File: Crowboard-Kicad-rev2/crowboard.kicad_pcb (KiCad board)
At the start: 2 copper layers, 251.9 x 118.8 mm, 75 parts, among them U1 Pico

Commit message: rev2
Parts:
- added J1: Conn_01x05, other_parts:pimoroni, F.Cu at (149.5, 120.6)
- added SW1: RotaryEncoder, Rotary_Encoder:RotaryEncoder_Alps_EC12E_Vertical_H20mm, F.Cu at (118.9, 112.6)
- added SW2: RotaryEncoder, Rotary_Encoder:RotaryEncoder_Alps_EC12E_Vertical_H20mm, F.Cu at (166.5, 112.7)
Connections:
- U1 pad 16: unconnected-(U1-Pad16) -> ENC0P1
- U1 pad 17: unconnected-(U1-Pad17) -> ENC0P2
- U1 pad 18: unconnected-(U1-Pad18) -> GND
- U1 pad 31: unconnected-(U1-Pad31) -> ENC1P2
- U1 pad 32: unconnected-(U1-Pad32) -> ENC1P1
- U1 pad 36: unconnected-(U1-Pad36) -> VCC
- U1 pad 4: unconnected-(U1-Pad4) -> SDA
- U1 pad 5: unconnected-(U1-Pad5) -> SCL
- U1 pad 8: unconnected-(U1-Pad8) -> GND1
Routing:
- net GND: track 0.00 -> 110.9 mm
- net SDA: track 0.00 -> 57.3 mm
- net SCL: track 0.00 -> 53.7 mm
- net VCC: track 0.00 -> 53.5 mm
- net ENC1P2: track 0.00 -> 53.0 mm, vias 0 -> 1
- net ENC1P1: track 0.00 -> 52.1 mm
- net ENC0P2: track 0.00 -> 44.3 mm, vias 0 -> 1
- net GND1: track 0.00 -> 44.0 mm
- net ENC0P1: track 0.00 -> 42.7 mm

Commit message: finrev2
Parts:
- added J2: Conn_01x04, Connector_PinHeader_2.54mm:PinHeader_1x04_P2.54mm_Vertical, F.Cu at (145.0, 100.6)
- moved J1 6.83 mm to (148.8, 113.8), turned to 180 degrees
- moved G*** 3.20 mm to (147.3, 114.3)
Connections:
- U1 pad 1: unconnected-(U1-Pad1) -> SDA1
- U1 pad 2: unconnected-(U1-Pad2) -> SCL1
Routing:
- net SDA1: track 0.00 -> 66.3 mm
- net SCL1: track 0.00 -> 60.3 mm, vias 0 -> 1
- net VCC: track 53.5 -> 88.2 mm, vias 0 -> 1
- net SDA: track 57.3 -> 88.3 mm, vias 0 -> 1
- net SCL: track 53.7 -> 83.4 mm, vias 0 -> 1
- net GND1: track 44.0 -> 71.6 mm
- net GND: track 110.9 -> 126.4 mm, vias 0 -> 1
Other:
- board text added: "ENDGAME"
- board text added: "MATERIAL"

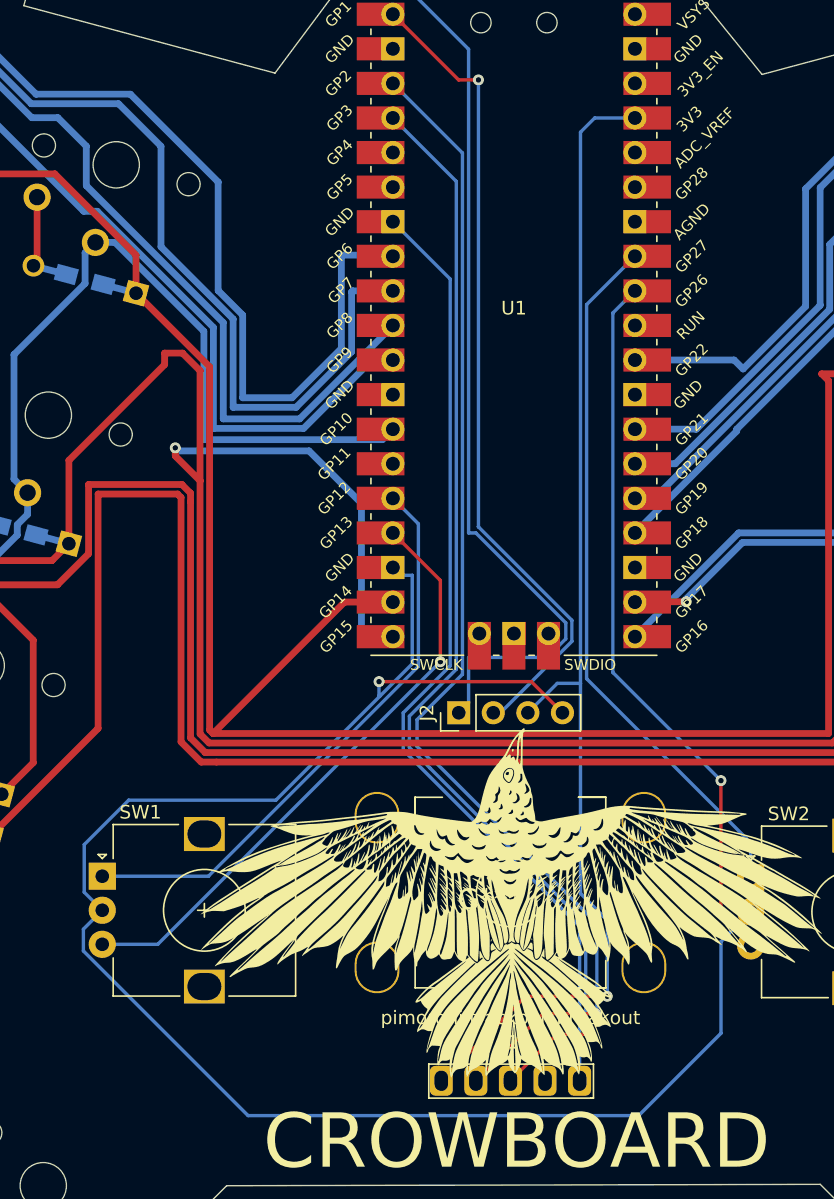
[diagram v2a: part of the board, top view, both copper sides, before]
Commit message: Removed Pimoroni Trackball
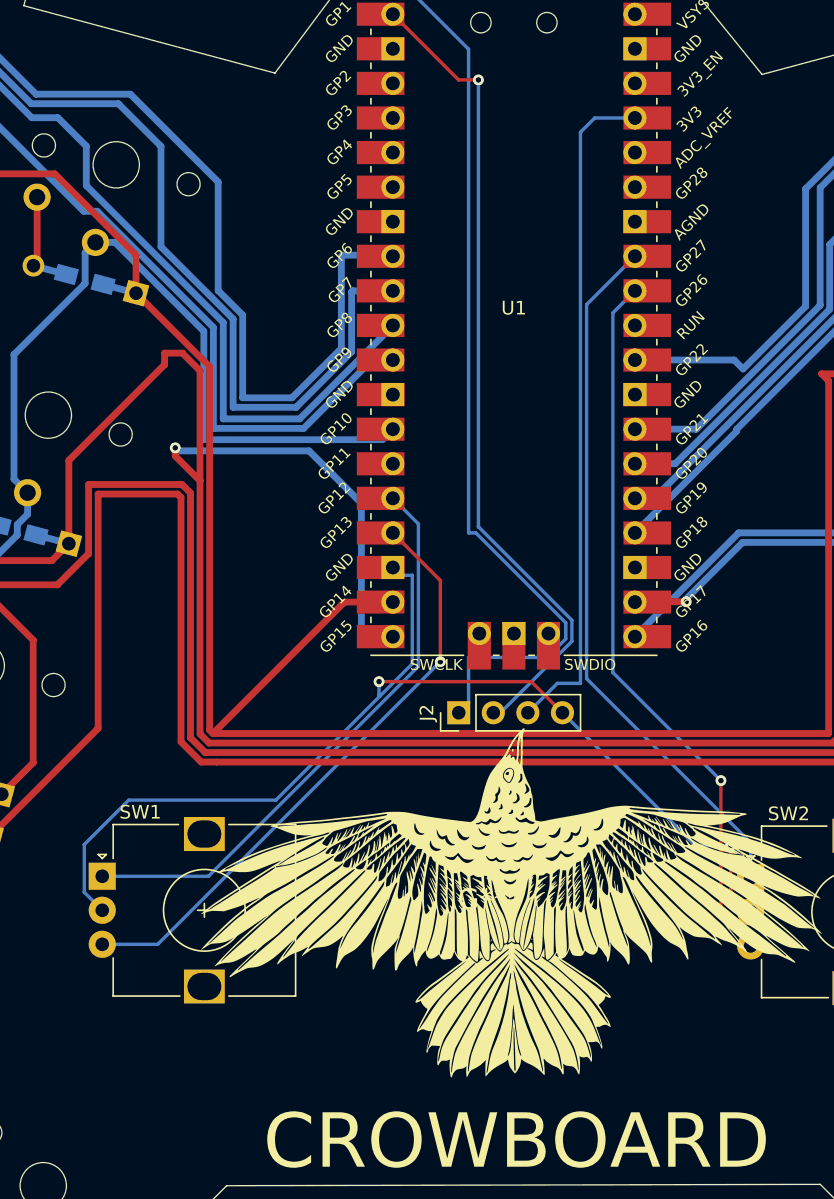
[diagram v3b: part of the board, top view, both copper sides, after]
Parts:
- removed J1: Conn_01x05, other_parts:pimoroni
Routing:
- net SDA: track 88.3 -> 0.00 mm, vias 1 -> 0
- net SCL: track 83.4 -> 0.00 mm, vias 1 -> 0
- net GND1: track 71.6 -> 0.00 mm
- net GND: track 126.4 -> 80.5 mm, vias 1 -> 2
- net VCC: track 88.2 -> 49.7 mm, vias 1 -> 0

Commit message: removed backup files
removed
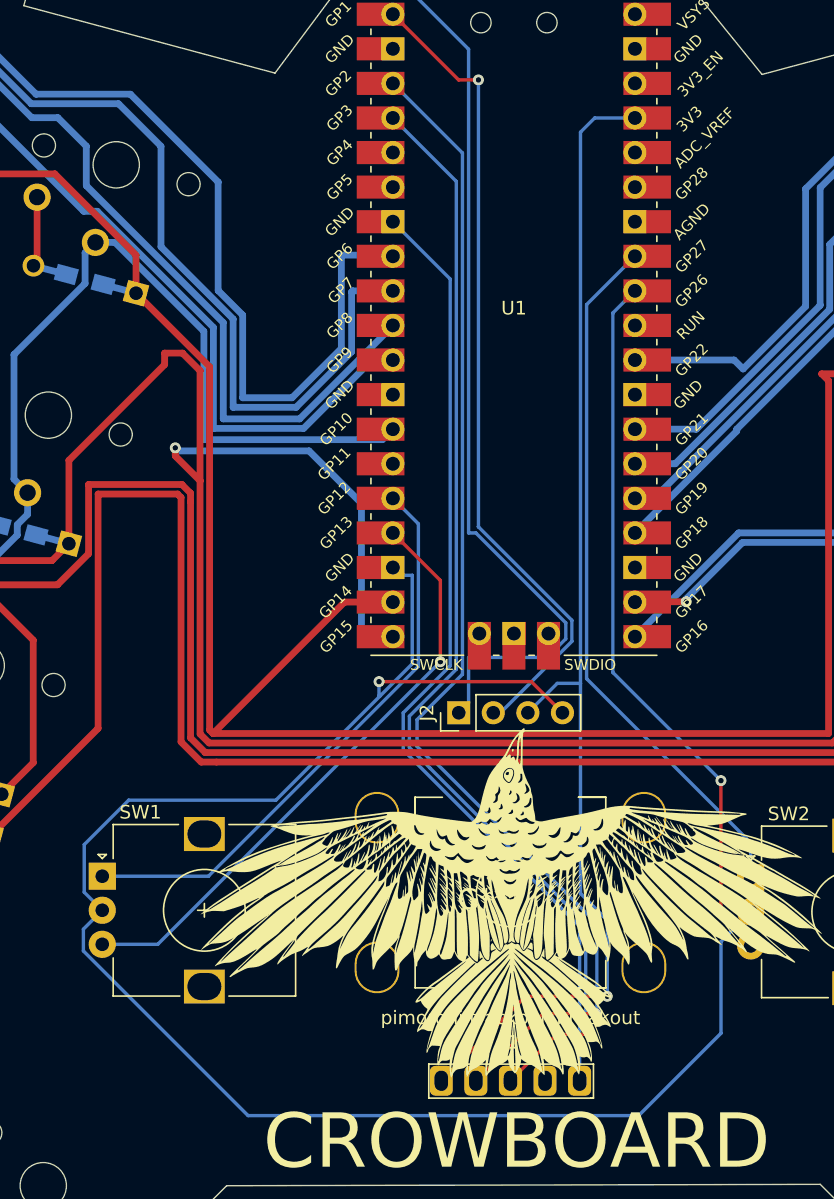
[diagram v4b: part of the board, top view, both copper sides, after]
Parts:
- added J1: Conn_01x05, other_parts:pimoroni, F.Cu at (148.8, 113.8)
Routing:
- net SDA: track 0.00 -> 88.3 mm, vias 0 -> 1
- net SCL: track 0.00 -> 83.4 mm, vias 0 -> 1
- net GND1: track 0.00 -> 71.6 mm
- net GND: track 80.5 -> 126.4 mm, vias 2 -> 1
- net VCC: track 49.7 -> 88.2 mm, vias 0 -> 1
